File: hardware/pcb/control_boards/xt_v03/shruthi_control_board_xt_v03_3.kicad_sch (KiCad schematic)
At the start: 50 parts, among them IC2 74HC165N, IC3 74HC165N, IC8 74595N, IC9 74HC165N, SW1 Encoder

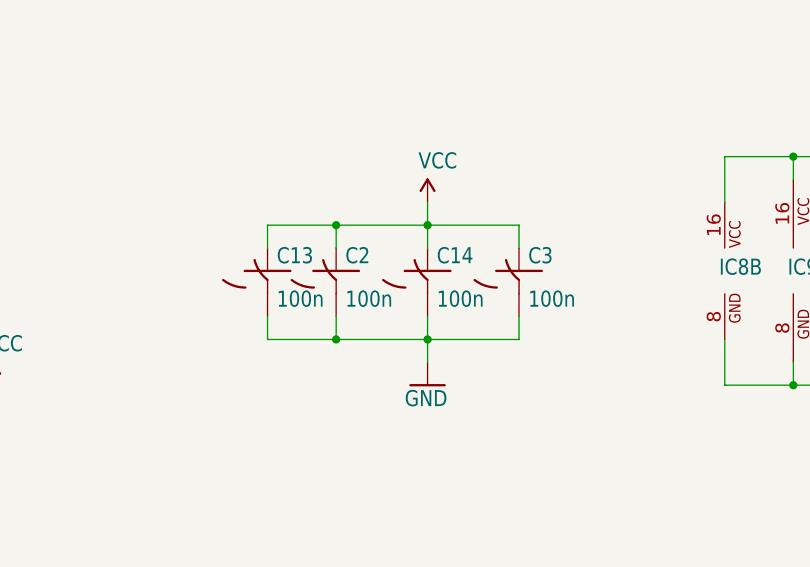
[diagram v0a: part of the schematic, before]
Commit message: update capacitors to use kicad symbols
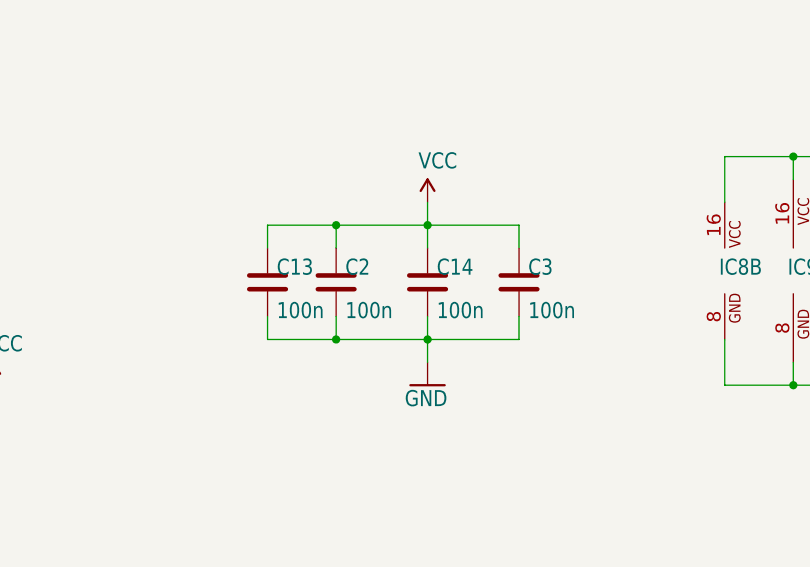
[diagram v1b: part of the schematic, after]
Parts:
- C13, C14, C2, C3: symbol shruthi_control_board_xt_v03-eagle-import:C-US025-024X044 -> Device:C
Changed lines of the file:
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@@
 	)
 	(symbol
-		(lib_id "shruthi_control_board_xt_v03-eagle-import:C-US025-024X044")
-		(at 340.36 218.44 0)
+		(lib_id "Device:C")
+		(at 340.36 219.71 0)
 		(unit 1)
 		(exclude_from_sim no)
@@
 		(dnp no)
 		(property "Reference" "C3"
-			(at 341.376 217.805 0)
+			(at 341.376 219.075 0)
 			(effects
 				(font
@@
 		)
 		(property "Value" "100n"
-			(at 341.376 222.631 0)
+			(at 341.376 223.901 0)
 			(effects
 				(font
@@
 		)
 		(property "Footprint" "shruthi_control_board_xt_v03:C025-024X044"
-			(at 340.36 218.44 0)
-			(effects
-				(font
-					(size 1.27 1.27)
-				)
-				(hide yes)
-			)
-		)
-		(property "Datasheet" ""
-			(at 340.36 218.44 0)
-			(effects
-				(font
-					(size 1.27 1.27)
-				)
-				(hide yes)
-			)
-		)
-		(property "Description" ""
-			(at 340.36 218.44 0)
+			(at 341.3252 223.52 0)
+			(effects
+				(font
+					(size 1.27 1.27)
+				)
+				(hide yes)
+			)
+		)
+		(property "Datasheet" "~"
+			(at 340.36 219.71 0)
+			(effects
+				(font
+					(size 1.27 1.27)
+				)
+				(hide yes)
+			)
+		)
+		(property "Description" "Unpolarized capacitor"
+			(at 340.36 219.71 0)
 			(effects
 				(font
@@
 	)
 	(symbol
-		(lib_id "shruthi_control_board_xt_v03-eagle-import:C-US025-024X044")
-		(at 330.2 218.44 0)
+		(lib_id "Device:C")
+		(at 330.2 219.71 0)
 		(unit 1)
 		(exclude_from_sim no)
@@
 		(dnp no)
 		(property "Reference" "C14"
-			(at 331.216 217.805 0)
+			(at 331.216 219.075 0)
 			(effects
 				(font
@@
 		)
 		(property "Value" "100n"
-			(at 331.216 222.631 0)
+			(at 331.216 223.901 0)
 			(effects
 				(font
@@
 		)
 		(property "Footprint" "shruthi_control_board_xt_v03:C025-024X044"
-			(at 330.2 218.44 0)
-			(effects
-				(font
-					(size 1.27 1.27)
-				)
-				(hide yes)
-			)
-		)
-		(property "Datasheet" ""
-			(at 330.2 218.44 0)
-			(effects
-				(font
-					(size 1.27 1.27)
-				)
-				(hide yes)
-			)
-		)
-		(property "Description" ""
-			(at 330.2 218.44 0)
+			(at 331.1652 223.52 0)
+			(effects
+				(font
+					(size 1.27 1.27)
+				)
+				(hide yes)
+			)
+		)
+		(property "Datasheet" "~"
+			(at 330.2 219.71 0)
+			(effects
+				(font
+					(size 1.27 1.27)
+				)
+				(hide yes)
+			)
+		)
+		(property "Description" "Unpolarized capacitor"
+			(at 330.2 219.71 0)
 			(effects
 				(font
@@
 	)
 	(symbol
-		(lib_id "shruthi_control_board_xt_v03-eagle-import:C-US025-024X044")
-		(at 320.04 218.44 0)
+		(lib_id "Device:C")
+		(at 320.04 219.71 0)
 		(unit 1)
 		(exclude_from_sim no)
@@
 		(dnp no)
 		(property "Reference" "C2"
-			(at 321.056 217.805 0)
+			(at 321.056 219.075 0)
 			(effects
 				(font
@@
 		)
 		(property "Value" "100n"
-			(at 321.056 222.631 0)
+			(at 321.056 223.901 0)
 			(effects
 				(font
@@
 		)
 		(property "Footprint" "shruthi_control_board_xt_v03:C025-024X044"
-			(at 320.04 218.44 0)
-			(effects
-				(font
-					(size 1.27 1.27)
-				)
-				(hide yes)
-			)
-		)
-		(property "Datasheet" ""
-			(at 320.04 218.44 0)
-			(effects
-				(font
-					(size 1.27 1.27)
-				)
-				(hide yes)
-			)
-		)
-		(property "Description" ""
-			(at 320.04 218.44 0)
+			(at 321.0052 223.52 0)
+			(effects
+				(font
+					(size 1.27 1.27)
+				)
+				(hide yes)
+			)
+		)
+		(property "Datasheet" "~"
+			(at 320.04 219.71 0)
+			(effects
+				(font
+					(size 1.27 1.27)
+				)
+				(hide yes)
+			)
+		)
+		(property "Description" "Unpolarized capacitor"
+			(at 320.04 219.71 0)
 			(effects
 				(font
@@
 	)
 	(symbol
-		(lib_id "shruthi_control_board_xt_v03-eagle-import:C-US025-024X044")
-		(at 312.42 218.44 0)
+		(lib_id "Device:C")
+		(at 312.42 219.71 0)
 		(unit 1)
 		(exclude_from_sim no)
@@
 		(dnp no)
 		(property "Reference" "C13"
-			(at 313.436 217.805 0)
+			(at 313.436 219.075 0)
 			(effects
 				(font
@@
 		)
 		(property "Value" "100n"
-			(at 313.436 222.631 0)
+			(at 313.436 223.901 0)
 			(effects
 				(font
@@
 		)
 		(property "Footprint" "shruthi_control_board_xt_v03:C025-024X044"
-			(at 312.42 218.44 0)
-			(effects
-				(font
-					(size 1.27 1.27)
-				)
-				(hide yes)
-			)
-		)
-		(property "Datasheet" ""
-			(at 312.42 218.44 0)
-			(effects
-				(font
-					(size 1.27 1.27)
-				)
-				(hide yes)
-			)
-		)
-		(property "Description" ""
-			(at 312.42 218.44 0)
-			(effects
-				(font
+			(at 313.3852 223.52 0)
+			(effects
+				(font
+					(size 1.27 1.27)
+				)
+				(hide yes)
+			)
+		)
+		(property "Datasheet" "~"
+			(at 312.42 219.71 0)
+			(effects
+				(font
+					(size 1.27 1.27)
+				)
+				(hide yes)
+			)
+		)
+		(property "Description" "Unpolarized capacitor"
+			(at 312.42 219.71 0)
+			(effects
+				(font
